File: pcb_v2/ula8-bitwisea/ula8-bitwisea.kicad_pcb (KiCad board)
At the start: 2 copper layers, 54.4 x 61 mm, 11 parts, among them J1 ula8a, U1 74LS32, U2 74LS32, U3 74LS244

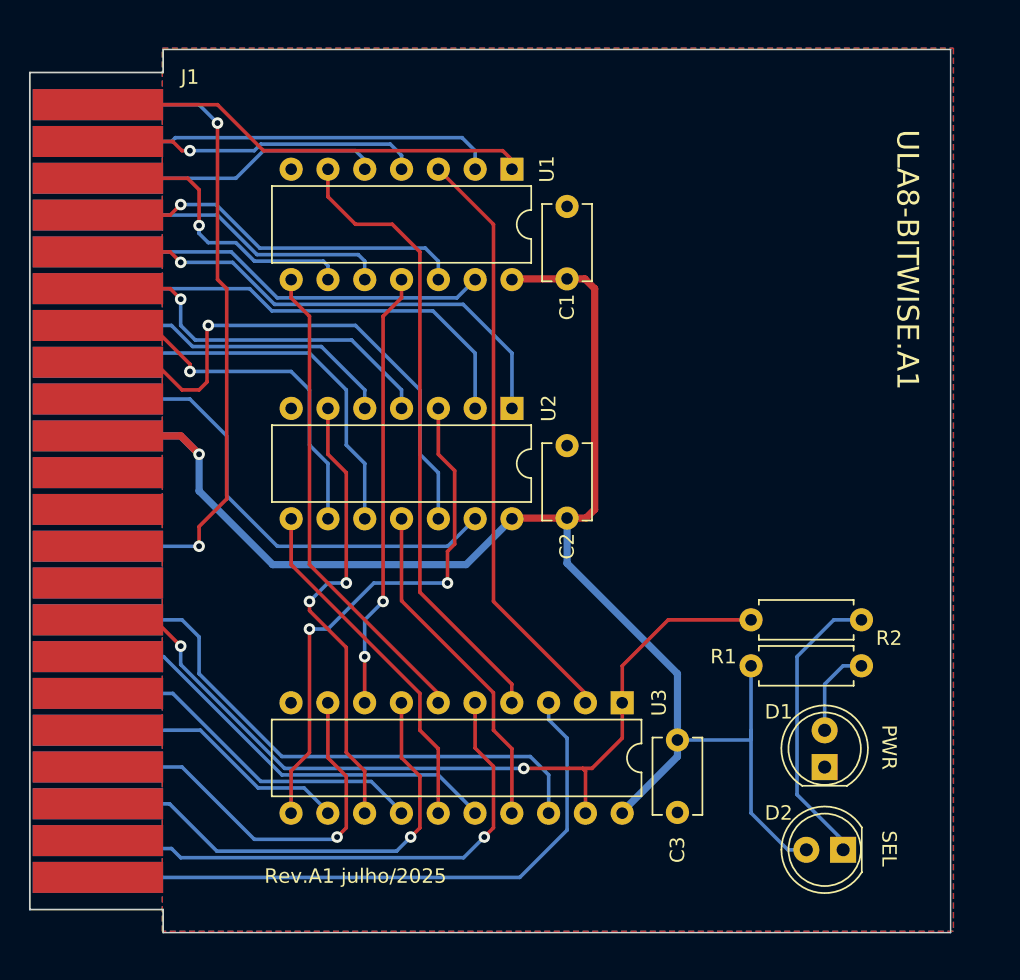
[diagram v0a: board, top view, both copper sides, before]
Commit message: alimentação movida para as extremidades do conector
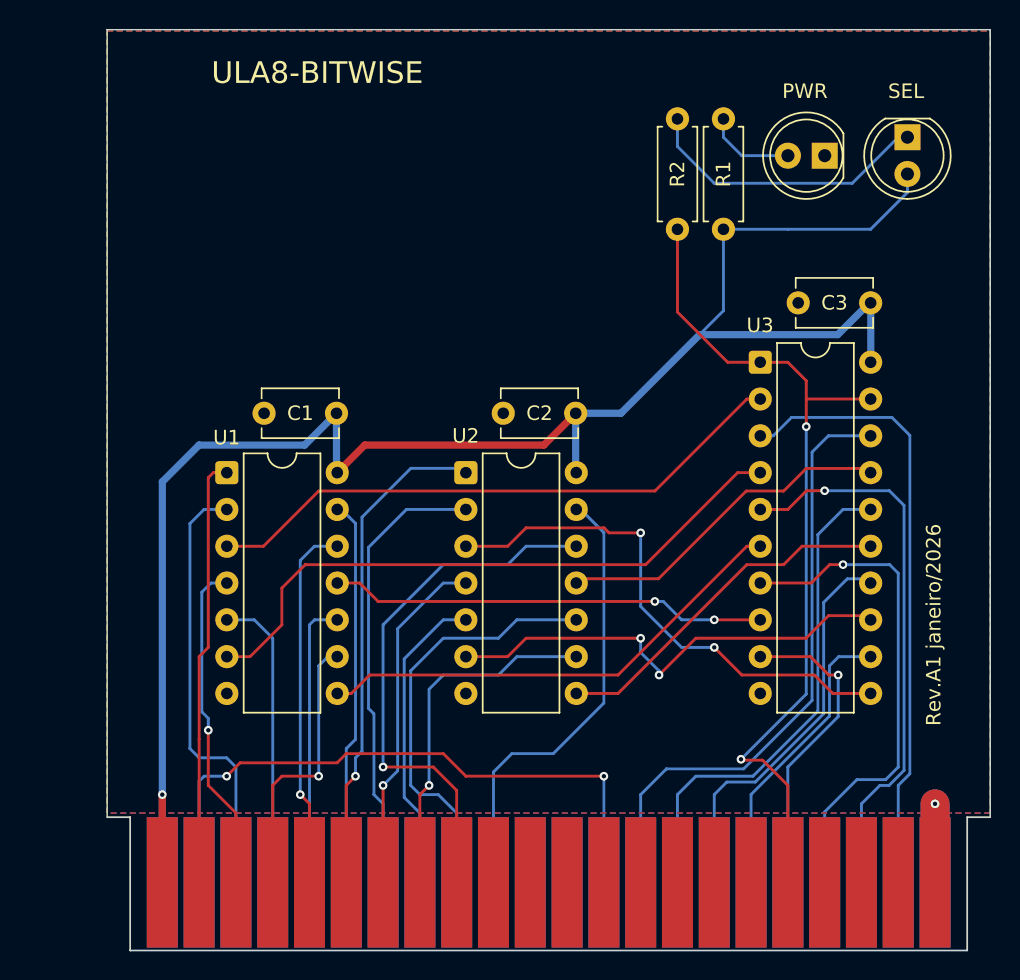
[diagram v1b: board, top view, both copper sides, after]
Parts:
- moved J1 53.9 mm to (37.5, 82.3), turned to 90 degrees
- moved D2 49.4 mm to (88.9, 30.8), turned to -90 degrees
- moved D1 42.2 mm to (83.2, 32.1), turned to 180 degrees
- moved R2 36.8 mm to (73.0, 29.6), turned to -90 degrees
- moved C3 36.1 mm to (81.4, 42.3), turned to 0 degrees
- moved R1 30.2 mm to (76.2, 37.2), turned to 90 degrees
- moved U1 28.7 mm to (41.9, 54.0), turned to 0 degrees
- moved U3 25.4 mm to (78.7, 46.4), turned to 0 degrees
- moved C1 25.3 mm to (44.5, 49.9), turned to 0 degrees
- moved U2 5.46 mm to (58.4, 54.0), turned to 0 degrees
- moved C2 4.94 mm to (61.0, 49.9), turned to 0 degrees
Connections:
- J1 pad 1: lower_bus0 -> +5V
- J1 pad 10: +5V -> unconnected-(J1-Pin_10-Pad10)
- J1 pad 11: GND -> unconnected-(J1-Pin_11-Pad11)
- J1 pad 15: n_select -> unconnected-(J1-Pin_15-Pad15)
- J1 pad 18: unconnected-(J1-Pad18) -> ~{select}
- J1 pad 2: lower_bus1 -> lower_bus0
- J1 pad 22: unconnected-(J1-Pad22) -> GND
- J1 pad 23: /carry -> +5V
- J1 pad 24: upper_bus0 -> carry
- J1 pad 25: upper_bus1 -> upper_bus0
- J1 pad 26: upper_bus2 -> upper_bus1
- J1 pad 27: upper_bus3 -> upper_bus2
- J1 pad 28: upper_bus4 -> upper_bus3
- J1 pad 29: upper_bus5 -> upper_bus4
- J1 pad 3: lower_bus2 -> lower_bus1
- J1 pad 30: upper_bus6 -> upper_bus5
- J1 pad 31: upper_bus7 -> upper_bus6
- J1 pad 32: +5V -> upper_bus7
- J1 pad 33: GND -> unconnected-(J1-Pin_33-Pad33)
- J1 pad 35: /carry -> carry
- J1 pad 36: unconnected-(J1-Pad36) -> ula_bus0
- J1 pad 37: ula_bus0 -> ula_bus1
- J1 pad 38: ula_bus1 -> ula_bus2
- J1 pad 39: ula_bus2 -> ula_bus3
- J1 pad 4: lower_bus3 -> lower_bus2
- J1 pad 40: ula_bus3 -> ula_bus4
- J1 pad 41: ula_bus4 -> ula_bus5
- J1 pad 42: ula_bus5 -> ula_bus6
- J1 pad 43: ula_bus6 -> ula_bus7
- J1 pad 44: ula_bus7 -> GND
- J1 pad 5: lower_bus4 -> lower_bus3
- J1 pad 6: lower_bus5 -> lower_bus4
- J1 pad 7: lower_bus6 -> lower_bus5
- J1 pad 8: lower_bus7 -> lower_bus6
- J1 pad 9: unconnected-(J1-Pad9) -> lower_bus7
- R2 pad 2: n_select -> ~{select}
- U3 pad 1: n_select -> ~{select}
- U3 pad 19: n_select -> ~{select}
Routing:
- net n_select: track 60.1 -> 0.00 mm, vias 2 -> 0
- net ~{select}: track 0.00 -> 59.5 mm, vias 0 -> 2
- net /carry: track 45.8 -> 0.00 mm, vias 2 -> 0
- net carry: track 0.00 -> 43.7 mm, vias 0 -> 2
- net GND: track 0.00 -> 10.9 mm, vias 0 -> 1
- net +5V: track 115.2 -> 123.6 mm
- net ula_bus4: track 28.6 -> 21.5 mm
- net ula_bus1: track 30.3 -> 34.7 mm
- net ula_bus2: track 24.1 -> 27.4 mm
- net ula_bus0: track 39.4 -> 41.9 mm
- net upper_bus0: track 27.8 -> 30.2 mm
- net lower_bus5: track 26.0 -> 23.7 mm
- net ula_bus3: track 18.0 -> 20.3 mm
- net upper_bus7: track 33.5 -> 31.5 mm
- net ula_bus5: track 33.3 -> 35.0 mm
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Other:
- board size 54.4 x 61 mm -> 61 x 54.4 mm
- board text added: "Rev.A1 janeiro/2026"
- board text added: "ULA8-BITWISE"
- board text removed: "Rev.A1 julho/2025"
- board text removed: "ULA8-BITWISE.A1"

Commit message: deslocando alimentação para as estremidades do conector; carry out em três estados (ativo apenas quando select)
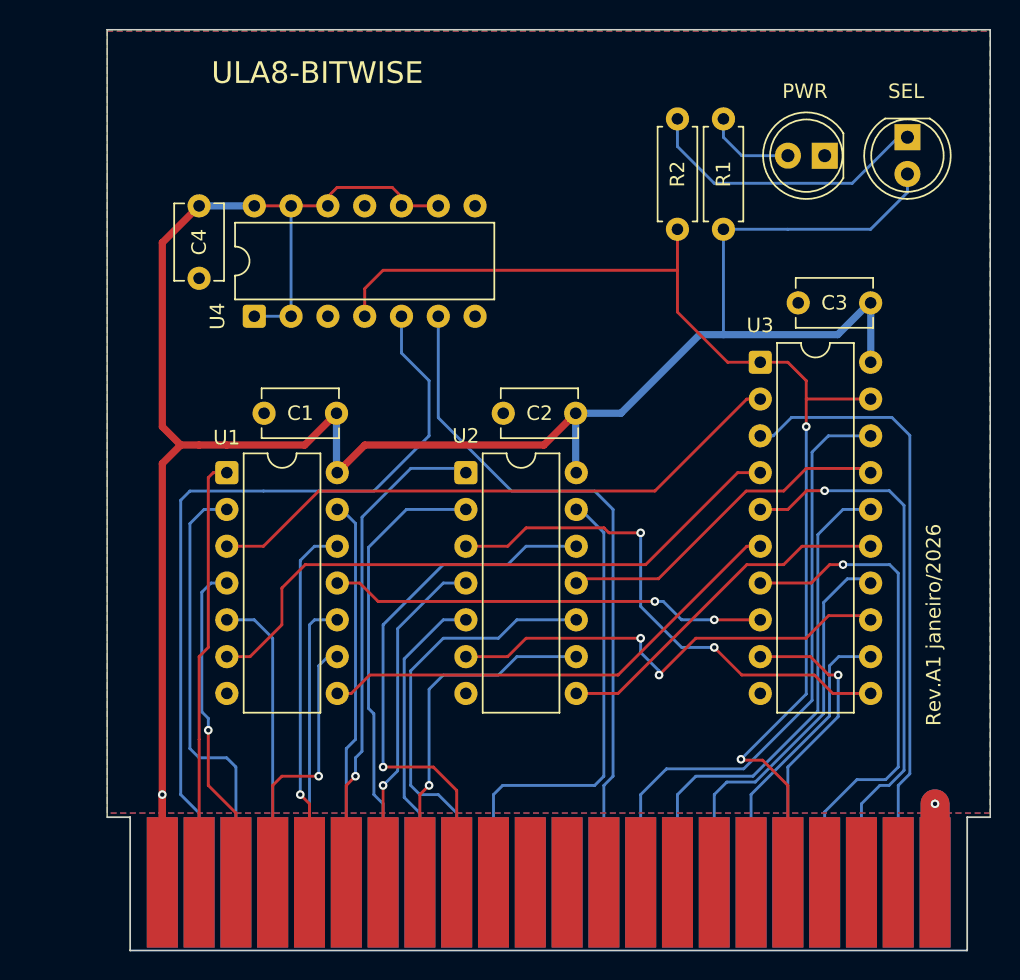
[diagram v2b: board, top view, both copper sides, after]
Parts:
- added C4: 100nF, Capacitor_THT:C_Disc_D5.1mm_W3.2mm_P5.00mm, F.Cu at (40.0, 40.6)
- added U4: 74LS125, Package_DIP:DIP-14_W7.62mm, F.Cu at (43.8, 43.2)
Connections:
- J1 pad 24: carry -> carry_in
- J1 pad 35: carry -> carry_out
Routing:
- net carry_in: track 0.00 -> 54.9 mm
- net +5V: track 123.6 -> 176.2 mm
- net carry_out: track 0.00 -> 47.7 mm
- net carry: track 43.7 -> 0.00 mm, vias 2 -> 0
- net ~{select}: track 59.5 -> 83.6 mm
- net upper_bus7: track 31.5 -> 33.6 mm
